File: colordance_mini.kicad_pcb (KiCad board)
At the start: 2 copper layers, 180 x 125 mm, 75 parts, among them J1 XLR3, J10 CONN_01X06, J11 CONN_01X04, J12 CONN_01X04, J13 CONN_01X03, J14 CONN_01X03, J15 CONN_01X03, J16 CONN_01X03, J17 CONN_01X04, J2 CONN_01X08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

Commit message: Add schematic and assembly sheet
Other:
- board text added: "6N137"
- board text added: "APA102"

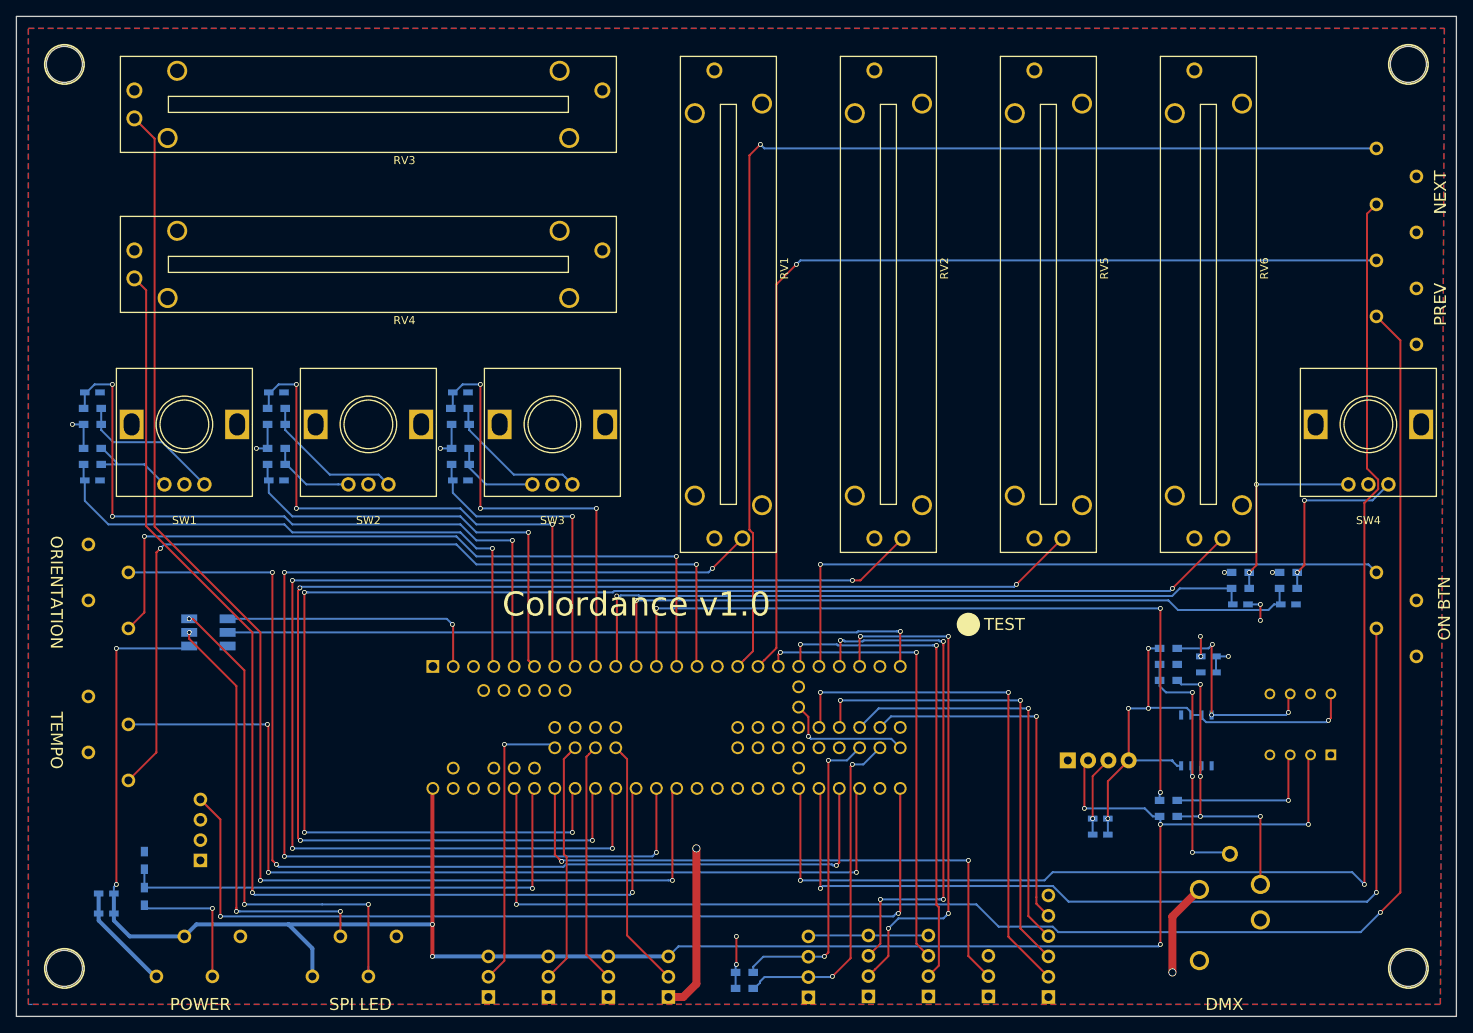
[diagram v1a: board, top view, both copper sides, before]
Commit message: Revision 1.1
- Fix Teensy footprint to not use pads
- Opto isolator gets 3v3 instead of 5v
- Separate ground for DMX side
- Fix DMX connector pinout
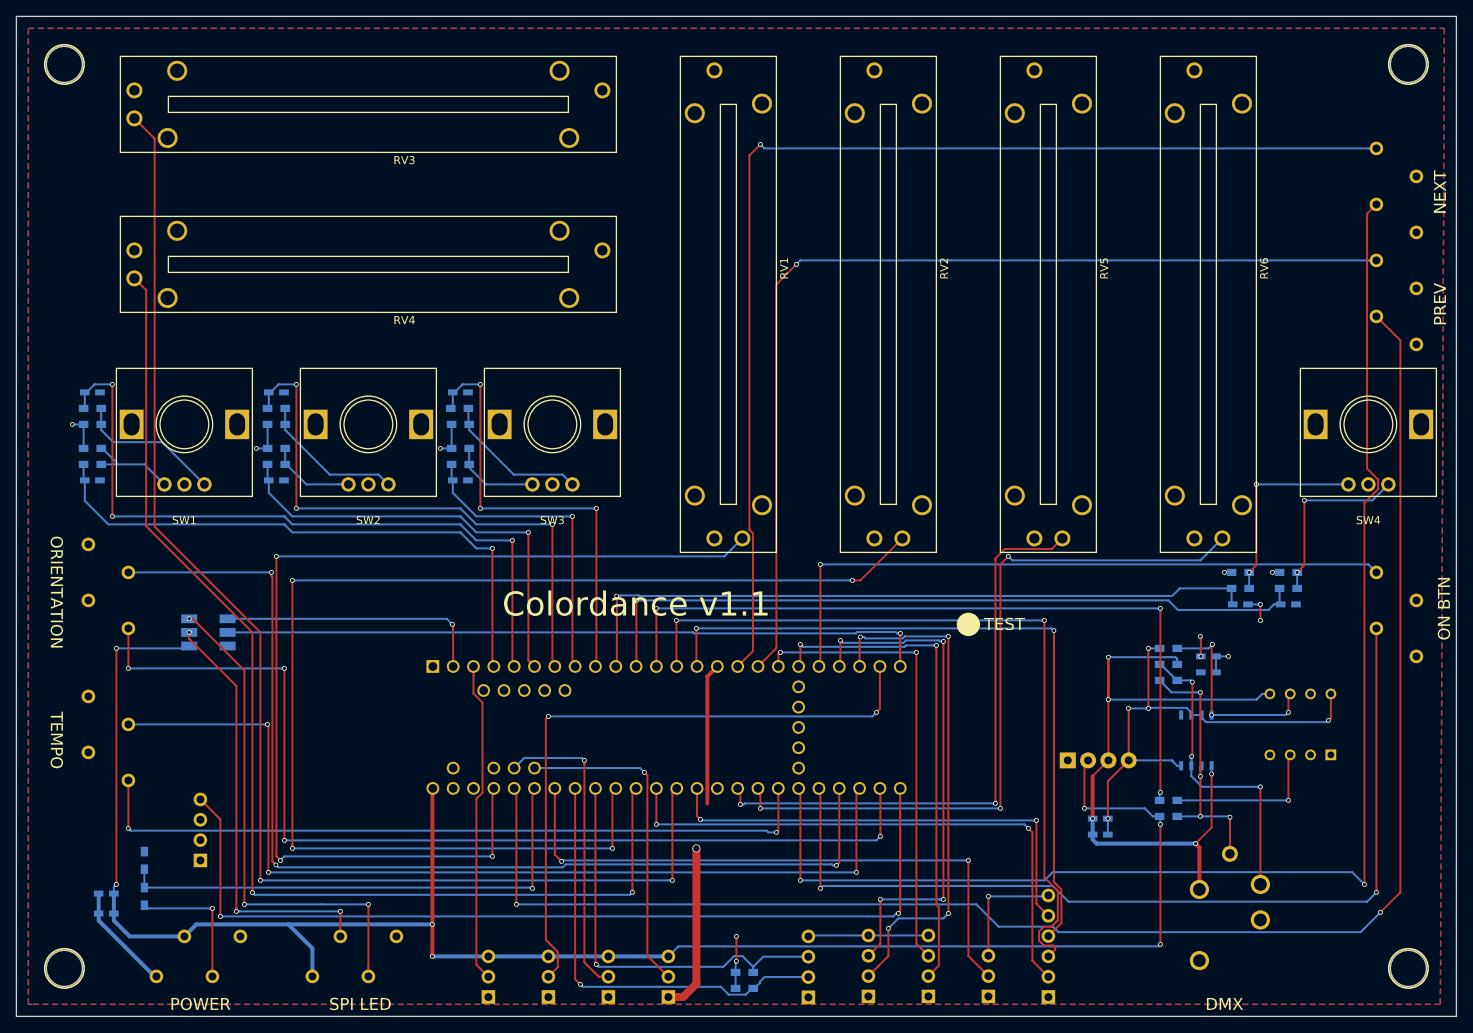
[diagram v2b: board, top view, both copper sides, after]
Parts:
- U4: footprint teensy:Teensy35_36 -> homebrew:Teensy35_36
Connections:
- C7 pad 2: GND -> GND_DMX
- C8 pad 2: GND -> GND_DMX
- J1 pad 1: GND -> GND_DMX
- R4 pad 2: Net-(J1-Pad2) -> Net-(J1-Pad3)
- R5 pad 1: Net-(J1-Pad3) -> Net-(J1-Pad2)
- R5 pad 2: GND -> GND_DMX
- U1 pad 5: GND -> GND_DMX
- U1 pad 6: Net-(J1-Pad2) -> Net-(J1-Pad3)
- U1 pad 7: Net-(J1-Pad3) -> Net-(J1-Pad2)
- U2 pad 3: GND -> GND_DMX
- U3 pad 2: +5V -> +3V3
- U3 pad 5: GND -> GND_DMX
- U4 pad 13: ORIENTATION -> AUX_MOSI
- U4 pad 14: TEMPO_TAP -> AUX_MISO
- U4 pad 15: Net-(U4-Pad15) -> +3V3
- U4 pad 23: Net-(U4-Pad23) -> MOTION_2
- U4 pad 3: Net-(U4-Pad3) -> MOTION_1
- U4 pad 31: Net-(U4-Pad31) -> ORIENTATION
- U4 pad 36: Net-(U4-Pad36) -> TEMPO_TAP
- U4 pad 37: Net-(U4-Pad37) -> PARAM
- U4 pad 38: Net-(U4-Pad38) -> DENSITY
- U4 pad 40: Net-(U4-Pad40) -> AUX_SCK
- U4 pad 42: TILT -> AUX_CS
- U4 pad 45: DENSITY -> SDA0
- U4 pad 46: PARAM -> SCL0
- U4 pad 50: Net-(U4-Pad50) -> TILT
- U4 pad 56: Net-(U4-Pad56) -> MOTION_3
- U4 pad 57: Net-(U4-Pad57) -> MOTION_4
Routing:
- net DENSITY: track 172.9 -> 74.1 mm, vias 4 -> 2
- net PARAM: track 186.7 -> 92.6 mm, vias 4 -> 3
- net GND_DMX: track 0.00 -> 88.3 mm, vias 0 -> 5
- net MOTION_2: track 30.3 -> 80.9 mm, vias 0 -> 2
- net AUX_MOSI: track 59.4 -> 97.8 mm
- net AUX_MISO: track 51.6 -> 88.8 mm, vias 1 -> 2
- net ORIENTATION: track 93.6 -> 126.7 mm, vias 2 -> 4
- net +5V: track 264.4 -> 237.1 mm, vias 8 -> 7
- net GND: track 62.5 -> 40.7 mm, vias 7 -> 5
- net TEMPO_TAP: track 111.7 -> 92.8 mm
- net TILT: track 149.2 -> 132.7 mm, vias 4 -> 3
- net +3V3: track 56.4 -> 72.7 mm
- net AUX_SCK: track 45.7 -> 58.6 mm, vias 1 -> 2
- net SCL0: track 42.4 -> 55.3 mm, vias 2 -> 1
- net SDA0: track 39.4 -> 51.5 mm, vias 2 -> 1
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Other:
- board text added: "Colordance v1.1"
- board text removed: "Colordance v1.0"

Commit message: Hardware revision v1.2:
- Switch power to Anderson connector
- Switch SPI LED connector to soldered 4-pin JST
- Add filter caps to the pots
- Add a few decoupling caps
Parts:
- removed R2: 3k3, Resistors_SMD:R_0603_HandSoldering
- removed R3: 1k, Resistors_SMD:R_0603_HandSoldering
- added BT1: BATTERY-20MM_SMD, Sparkfun-Batteries:BATTCON_20MM, B.Cu at (124.8, 77.8)
- added C15: .1uF, Capacitor_SMD:C_0603_1608Metric_Pad1.05x0.95mm_HandSolder, B.Cu at (107.4, 108.0)
- added C16: .1uF, Capacitor_SMD:C_0603_1608Metric_Pad1.05x0.95mm_HandSolder, B.Cu at (126.6, 109.6)
- added C17: .1uF, Capacitor_SMD:C_0603_1608Metric_Pad1.05x0.95mm_HandSolder, B.Cu at (35.6, 55.4)
- added C18: .1uF, Capacitor_SMD:C_0603_1608Metric_Pad1.05x0.95mm_HandSolder, B.Cu at (35.6, 75.4)
- added C19: .1uF, Capacitor_SMD:C_0603_1608Metric_Pad1.05x0.95mm_HandSolder, B.Cu at (150.4, 101.6)
- added C20: .1uF, Capacitor_SMD:C_0603_1608Metric_Pad1.05x0.95mm_HandSolder, B.Cu at (164.5, 106.0)
- added C21: 1uF, Capacitor_SMD:C_0603_1608Metric_Pad1.05x0.95mm_HandSolder, B.Cu at (178.5, 120.8)
- added C22: 1uF, Capacitor_SMD:C_0603_1608Metric_Pad1.05x0.95mm_HandSolder, B.Cu at (45.0, 119.6)
- added C23: 1uF, Capacitor_SMD:C_0603_1608Metric_Pad1.05x0.95mm_HandSolder, B.Cu at (73.4, 159.6)
- J3: footprint homebrew:1985218_phoenix_4pos_3.5mm -> Connector_PinHeader_2.54mm:PinHeader_1x04_P2.54mm_Vertical
- J4: value CONN_01X03 -> Anderson_two_redblack; footprint homebrew:1985218_phoenix_4pos_3.5mm -> homebrew:Anderson_1337G3_straight_two
- moved J3 12.6 mm to (70.6, 159.2), turned to 90 degrees
- moved J4 5.93 mm to (44.4, 158.4)
- moved C13 5.81 mm to (38.0, 148.2)
- moved C14 5.81 mm to (38.0, 150.7)
- moved J5 0.45 mm to (43.6, 144.3)
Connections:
- J3 pad 2: Net-(D1-Pad5) -> Net-(D1-Pad6)
- J3 pad 3: Net-(D1-Pad6) -> Net-(D1-Pad5)
- J4 pad 1: GND -> +5V
- J4 pad 2: +5V -> GND
- J5 pad 3: Net-(J5-Pad3) -> (no net)
- U1 pad 1: Net-(U1-Pad1) -> (no net)
- U3 pad 7: Net-(U3-Pad7) -> (no net)
- U4 pad 1: Net-(U4-Pad1) -> (no net)
- U4 pad 28: Net-(U4-Pad28) -> (no net)
- U4 pad 29: Net-(U4-Pad29) -> (no net)
- U4 pad 39: Net-(U4-Pad39) -> (no net)
- U4 pad 48: VBATT_DIV -> (no net)
- U4 pad 51: Net-(U4-Pad51) -> (no net)
- U4 pad 54: Net-(U4-Pad54) -> (no net)
- U4 pad 55: Net-(U4-Pad55) -> (no net)
- U4 pad 58: Net-(U4-Pad58) -> (no net)
- U4 pad 59: Net-(U4-Pad59) -> (no net)
- U4 pad 60: Net-(U4-Pad60) -> (no net)
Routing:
- net VBATT_DIV: track 63.4 -> 0.00 mm, vias 1 -> 0
- net Net-(BT1-Pad1): track 0.00 -> 38.5 mm, vias 0 -> 1
- net +BATT: track 17.2 -> 0.00 mm, vias 1 -> 0
- net VDMX: track 62.3 -> 69.4 mm
- net Net-(D1-Pad5): track 53.4 -> 60.3 mm
- net +5V: track 237.1 -> 241.1 mm, vias 7 -> 6
- net GND_DMX: track 88.3 -> 91.3 mm
- net DENSITY: track 74.1 -> 76.9 mm
- net WIDTH: track 143.8 -> 146.7 mm
- net PAN: track 165.0 -> 167.8 mm
- net TILT: track 132.7 -> 134.7 mm
- net PARAM: track 92.6 -> 94.4 mm
- net GND: track 40.7 -> 41.5 mm
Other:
- board text added: "BOOST"
- board text added: "Colordance v1.2"
- board text added: "ORIENT"
- board text added: "RANDOM"
- board text removed: "12V"
- board text removed: "Colordance v1.1"
